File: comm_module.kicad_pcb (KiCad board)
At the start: 4 copper layers, 112.4 x 100.1 mm, 74 parts, among them J1 USB-231-ARY, J2 PH2.54-01-03PZS, J3 U.FL-R-SMT-1(80), J4 U.FL-R-SMT-1(80), J5 U.FL-R-SMT-1(80), J6 U.FL-R-SMT-1(80), J7 S3B-ZR-SM4A-TF(LF)(SN), J8 SMN-305-ARP7, J9 U.FL-R-SMT-1(80), Q1 BSS138PW,115, U1 MIC29302WU, U2 SIM7600E, U3 TXU0202DCUR, U4 TCA9406DCUR, X1 WJ500V-5.08-2P-14-00A

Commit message: First no error draft
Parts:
- removed J2: PH2.54-01-03PZS, pepy_sym_lib:[2x3_PIN_HEADER_STR]XUNPU PH2.54-01-03PZS
- removed J7: S3B-ZR-SM4A-TF(LF)(SN), pepy_sym_lib:[JST_1X3P_1_5MM_R_ANGLE]JST S3B-ZR-SM4A-TF(LF)(SN)
- removed R20: 0201WMF1002TEE, pepy_sym_lib:[RES_SMD_0201_0603Metric]
- added C26: CC0201KRX5R6BB104, pepy_sym_lib:[CAP_SMD_0201_0603Metric], F.Cu at (79.7, 86.3)
- added C27: CC0402KRX7R7BB104, pepy_sym_lib:[CAP_SMD_0402_1005Metric], F.Cu at (85.1, 55.7)
- added J10: PZ254V-11-06P, pepy_sym_lib:[6P_HEADER_STR]XFCN PZ254V-11-06P, F.Cu at (117.5, 50.0)
- added R24: 0805W8F1004T5E, pepy_sym_lib:[RES_SMD_0805_2012Metric], F.Cu at (69.8, 71.1)
- added R25: 0805W8F0000T5E, pepy_sym_lib:[RES_SMD_0805_2012Metric], F.Cu at (81.5, 56.5)
- added R26: 0402WGF2201TCE, pepy_sym_lib:[RES_SMD_0402_1005Metric], F.Cu at (115.0, 53.8)
- added R27: 0402WGF2201TCE, pepy_sym_lib:[RES_SMD_0402_1005Metric], F.Cu at (119.6, 50.8)
- added R28: 0805W8F0000T5E, pepy_sym_lib:[RES_SMD_0805_2012Metric], F.Cu at (81.5, 54.8)
- added TP1: DCD, pepy_sym_lib:[TEST_POINT]TestPoint_Pad_D1.0mm, F.Cu at (94.9, 55.3)
- added TP2: RI, pepy_sym_lib:[TEST_POINT]TestPoint_Pad_D1.0mm, F.Cu at (94.9, 52.4)
- added TP3: DTR, pepy_sym_lib:[TEST_POINT]TestPoint_Pad_D1.0mm, F.Cu at (91.6, 55.3)
- added TP4: RTS, pepy_sym_lib:[TEST_POINT]TestPoint_Pad_D1.0mm, F.Cu at (100.3, 49.7)
- added TP5: CTS, pepy_sym_lib:[TEST_POINT]TestPoint_Pad_D1.0mm, F.Cu at (98.3, 50.7)
- added TP6: SIM_STAT, pepy_sym_lib:[TEST_POINT]TestPoint_Pad_D1.0mm, F.Cu at (114.3, 79.2)
- added TP7: nRST, pepy_sym_lib:[TEST_POINT]TestPoint_Pad_D1.0mm, F.Cu at (78.2, 61.8)
- C16: value CC1206KKX7RDBB102 -> CC0201KRX5R6BB104; footprint pepy_sym_lib:[CAP_SMD_1206_3216Metric] -> pepy_sym_lib:[CAP_SMD_0201_0603Metric]
- J3, J4, J5, J6, J9: value U.FL-R-SMT-1(80) -> U.FLRSMT1
- R10: value RC0201FR-0733RL -> 0805W8F0000T5E; footprint pepy_sym_lib:[RES_SMD_0201_0603Metric] -> pepy_sym_lib:[RES_SMD_0805_2012Metric]
- R15: value 0805W8F1004T5E -> 0402WGF2201TCE; footprint pepy_sym_lib:[RES_SMD_0805_2012Metric] -> pepy_sym_lib:[RES_SMD_0402_1005Metric]
- R2: value 0402WGF0000TCE -> 0402WGF2201TCE
- R6: value RC0201FR-071ML -> 0805W8F0000T5E; footprint pepy_sym_lib:[RES_SMD_0201_0603Metric] -> pepy_sym_lib:[RES_SMD_0805_2012Metric]
- moved R2 69.6 mm to (123.4, 54.0), turned to 0 degrees
- moved C16 63.7 mm to (79.2, 79.3)
- moved R6 39.2 mm to (81.5, 58.2), turned to 180 degrees
- moved C1 37.6 mm to (76.6, 35.1), turned to 0 degrees
- moved R15 35.0 mm to (123.4, 51.2)
- moved D2 34.7 mm to (70.9, 32.0), turned to -90 degrees
- moved C3 33.4 mm to (72.7, 33.5), turned to -90 degrees
- moved R10 31.3 mm to (81.5, 53.1)
- moved R4 30.9 mm to (68.5, 32.1), turned to 0 degrees
- moved R5 28.7 mm to (66.5, 32.1), turned to 0 degrees
- moved R1 27.5 mm to (66.7, 42.2)
- moved C20 24.6 mm to (57.8, 75.7), turned to 180 degrees
- moved C25 23.9 mm to (121.1, 50.0), turned to 90 degrees
- moved C15 23.4 mm to (114.1, 56.6), turned to 180 degrees
- moved D1 20.7 mm to (63.9, 52.8)
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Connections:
- net /D+_COMM renamed /DCOMM+
- net /D-_COMM renamed /DCOMM-
- net Net-(D3-I/O1-Pad1) renamed /DFILT-
- net Net-(D3-I/O2-Pad3) renamed /DFILT+
- C10 pad 2: VDD_3V3 -> /1V8_COMM
- C11 pad 2: Net-(C11-Pad2) -> /MAIN_ANT
- C12 pad 2: Net-(C12-Pad2) -> /AUX_ANT
- C15 pad 2: /1V8_COMM -> /VDD_3V3
- C16 pad 1: Earth_UART -> GND
- C16 pad 2: GND -> /1V8_COMM
- C25 pad 1: VDD_3V3 -> /VDD_3V3
- D5 pad 1: /SIM_DATA -> /SIM_VCC
- D5 pad 3: /SIM_VCC -> /SIM_RST
- D5 pad 4: /SIM_RST -> /SIM_CLK
- D5 pad 5: /SIM_CLK -> /SIM_DATA
- Q1 pad 1: /NETFLIGHT -> /NETLIGHT
- R10 pad 1: /SIM_VCC -> Net-(C27-Pad2)
- R10 pad 2: Net-(U2A-USIM_VDD) -> /VDD_3V3
- R15 pad 1: Earth_UART -> /COMM_SCL
- R15 pad 2: GND -> /1V8_COMM
- R16 pad 2: /1V8_COMM -> /VDD_AUX
- R18 pad 2: /SIM_VCC -> Net-(C27-Pad2)
- R2 pad 1: /EN -> /COMM_SDA
- R2 pad 2: Net-(U1-EN) -> /1V8_COMM
- R21 pad 2: /NETFLIGHT -> /NETLIGHT
- R22 pad 2: /NETFLIGHT -> /NETLIGHT
- R23 pad 2: VDD_3V3 -> /VDD_COMM
- R6 pad 1: Earth_USB -> Net-(C27-Pad2)
- R6 pad 2: GND -> /1V8_COMM
- R7 pad 1: Net-(C11-Pad2) -> /MAIN_ANT
- R8 pad 1: Net-(C12-Pad2) -> /AUX_ANT
- U2 pad 20: Net-(U2A-USIM_VDD) -> /SIM_VCC
- U2 pad 4: /nRST -> Net-(U2A-RESET)
- U2 pad 44: unconnected-(U2B-VDD_AUX-Pad44) -> /VDD_AUX
- U3 pad 1: /M_RX_S_TX_1V8 -> /M_TX_S_RX
- U3 pad 3: VDD_3V3 -> /1V8_COMM
- U3 pad 4: /M_RX_S_TX -> /M_TX_S_RX_1V8
- U3 pad 5: /M_TX_S_RX -> /M_RX_S_TX_1V8
- U3 pad 6: VDD_3V3 -> /1V8_COMM
- U3 pad 7: /1V8_COMM -> /VDD_3V3
- U3 pad 8: /M_TX_S_RX_1V8 -> /M_RX_S_TX
- U4 pad 6: Net-(U4-OE) -> /1V8_COMM
- U4 pad 7: VDD_3V3 -> /VDD_3V3
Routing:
- net GND: track 0.00 -> 118.3 mm, vias 0 -> 86
- net /1V8_COMM: track 0.00 -> 96.1 mm
- net /VDD_3V3: track 0.00 -> 74.4 mm
- net /VDD_COMM: track 0.00 -> 48.4 mm, vias 0 -> 22
- net Earth_SIM: track 0.00 -> 45.4 mm
- net /VBUS: track 0.00 -> 38.5 mm, vias 0 -> 1
- net /COMM_SCL: track 0.00 -> 34.7 mm, vias 0 -> 2
- net /COMM_SDA: track 0.00 -> 29.1 mm, vias 0 -> 2
- net /M_RX_S_TX_1V8: track 0.00 -> 22.6 mm
- net /SIM_VCC: track 0.00 -> 21.4 mm
- net Earth_USB: track 0.00 -> 21.1 mm
- net /VDD_AUX: track 0.00 -> 19.6 mm
- net /DCOMM-: track 0.00 -> 19.1 mm
- net /DCOMM+: track 0.00 -> 19.1 mm
- net /SIM_DATA: track 0.00 -> 18.3 mm, vias 0 -> 2
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- added copper zone on B.Cu, net /VBUS
- added copper zone on F.Cu, net /VBUS
- added copper zone on B.Cu, net /VDD_COMM
- added copper zone on F.Cu, net /VDD_COMM
- added copper zone on In1.Cu, net GND
- added copper zone on In2.Cu, net GND
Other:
- board size 112.4 x 100.1 mm -> 73.7 x 65.6 mm
- board text added: "0"
- board text added: "0 mm"
- board text added: "0.01 mm"
- board text added: "0.0152 mm"
- board text added: "0.02"
- board text added: "0.035 mm"
- board text added: "0.0994 mm"
- board text added: "1"
- board text added: "1.265 mm"
- board text added: "3.3"
- board text added: "4.1"
- board text added: "4.5"
- board text added: "B.Cu"
- board text added: "B.Mask"
- board text added: "B.Paste"
- board text added: "B.Silkscreen"
- board text added: "Bottom Silk Screen"
- board text added: "Bottom Solder Mask"
- board text added: "Bottom Solder Paste"
- board text added: "Color"
- board text added: "Dielectric"
- board text added: "Epsilon R"
- board text added: "F.Cu"
- board text added: "F.Mask"
- board text added: "F.Paste"
- board text added: "F.Silkscreen"
- board text added: "FR4"
- board text added: "In1.Cu"
- board text added: "In2.Cu"
- board text added: "Layer Name"
- board text added: "Loss Tangent"
- board text added: "Material"
- board text added: "Not specified"
- board text added: "Thickness (mm)"
- board text added: "Top Silk Screen"
- board text added: "Top Solder Mask"
- board text added: "Top Solder Paste"
- board text added: "Type"
- board text added: "copper"
- board text added: "core"
- board text added: "prepreg"

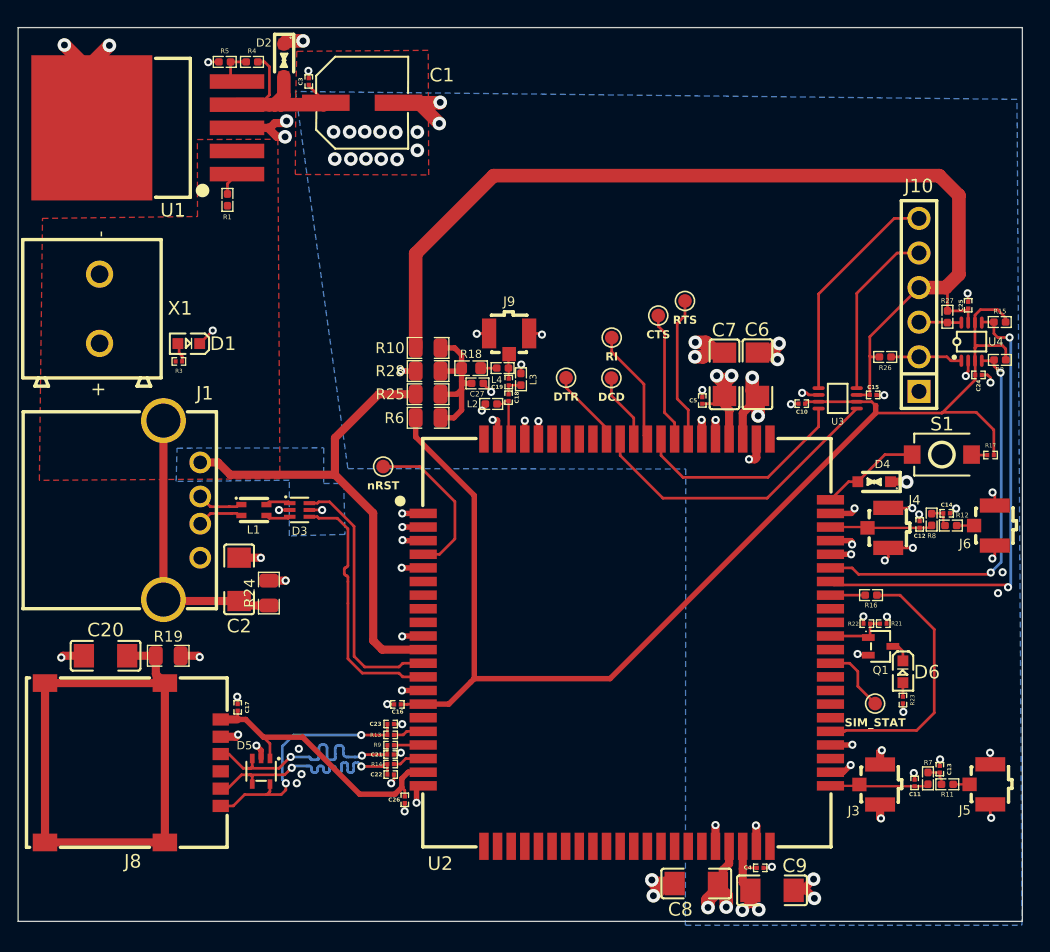
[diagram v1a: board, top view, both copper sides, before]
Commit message: Reannotation
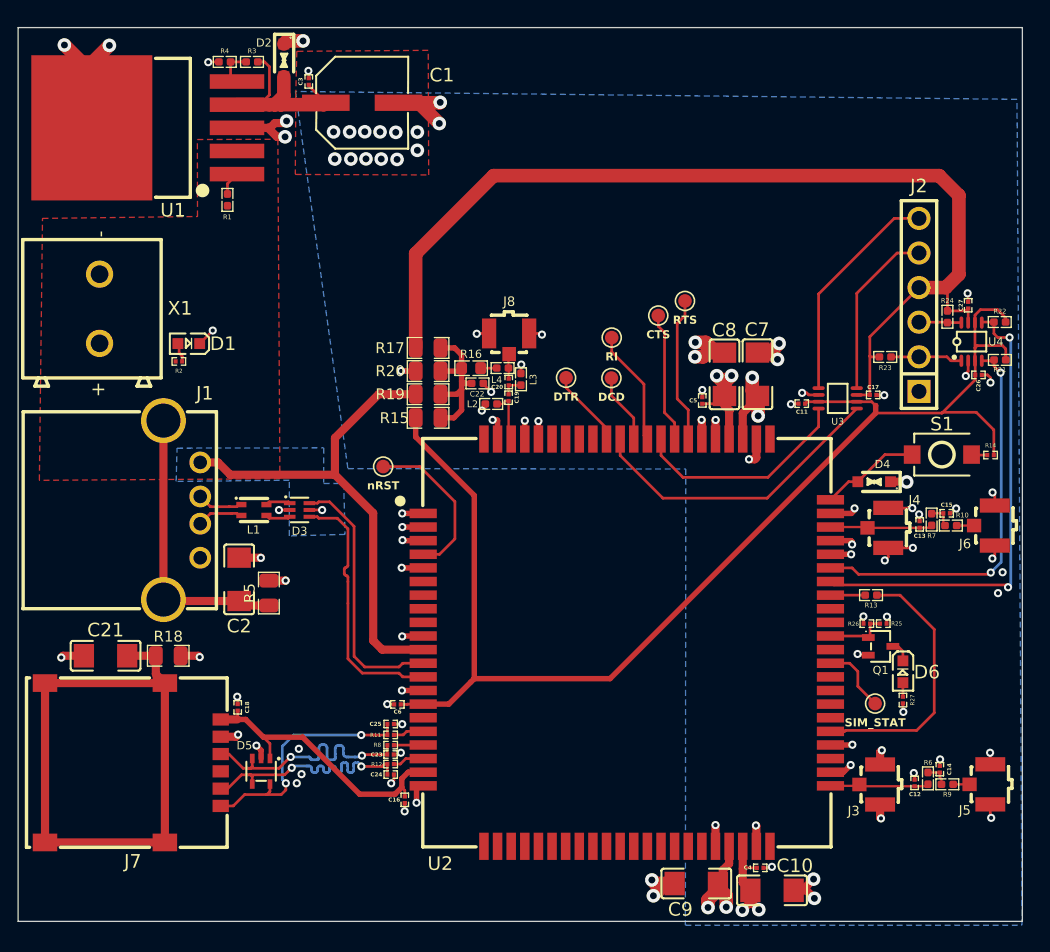
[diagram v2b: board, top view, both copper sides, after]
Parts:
- renumbered C9 to C10, C10 to C11, C11 to C12, C12 to C13, C13 to C14, C14 to C15, C26 to C16, C15 to C17, C17 to C18, C18 to C19, C19 to C20, C20 to C21, C27 to C22, C21 to C23, C22 to C24, C23 to C25, C24 to C26, C25 to C27, C16 to C6, C6 to C7, C7 to C8, C8 to C9, J10 to J2, J8 to J7, J9 to J8, R12 to R10, R13 to R11, R14 to R12, R16 to R13, R17 to R14, R6 to R15, R18 to R16, R10 to R17, R19 to R18, R25 to R19, R3 to R2, R28 to R20, R2 to R21, R15 to R22, R26 to R23, R27 to R24, R21 to R25, R22 to R26, R23 to R27, R4 to R3, R5 to R4, R24 to R5, R7 to R6, R8 to R7, R9 to R8, R11 to R9, TP7 to TP6, TP6 to TP7

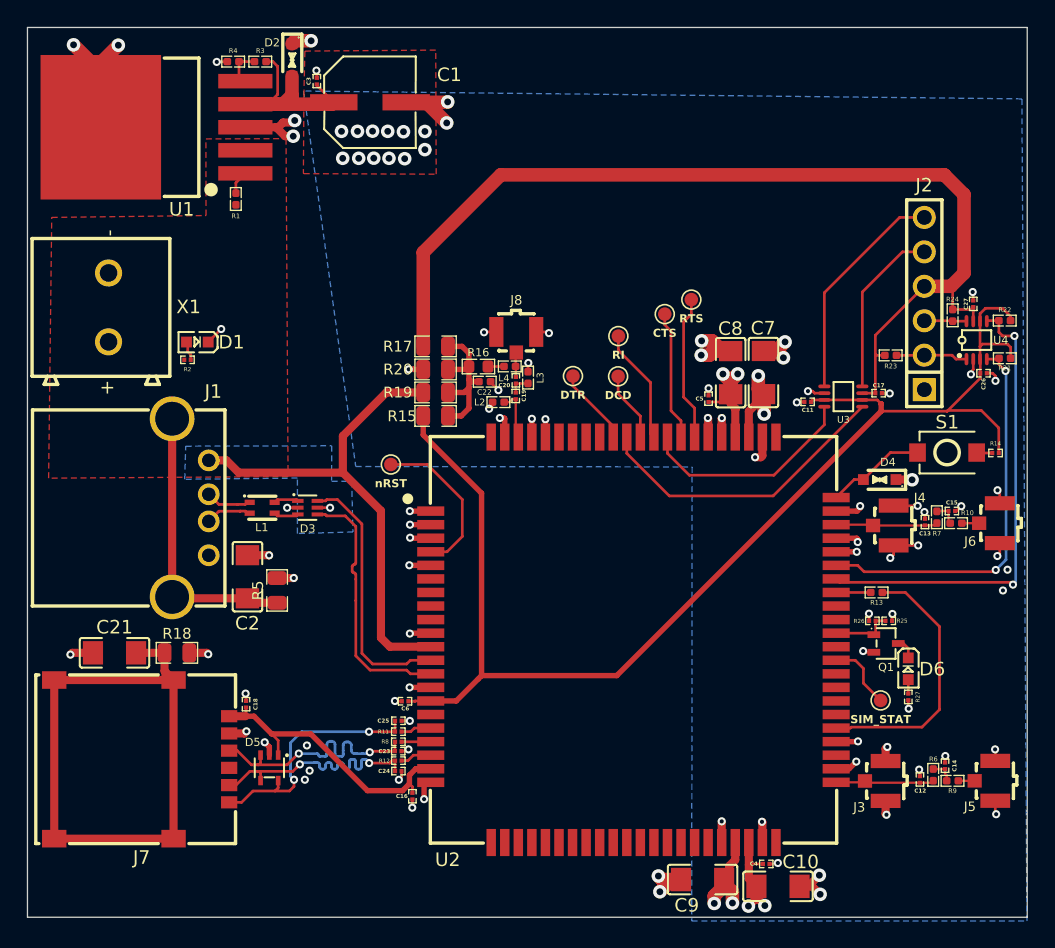
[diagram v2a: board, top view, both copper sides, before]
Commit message: Antenna polygon fixes and refinements
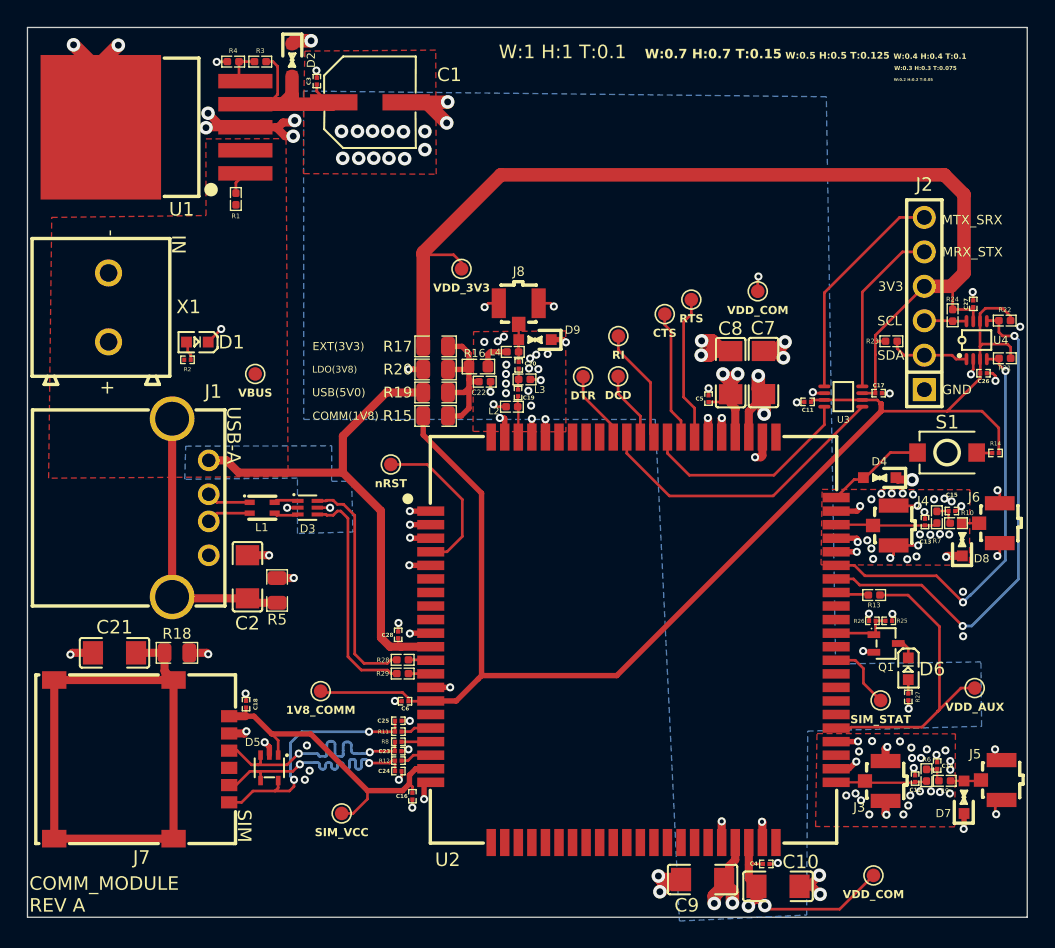
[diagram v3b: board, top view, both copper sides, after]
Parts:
- added C28: CC0201KRX5R6BB104, pepy_sym_lib:[CAP_SMD_0201_0603Metric], F.Cu at (78.7, 74.4)
- added D7: ESD56151W05, pepy_sym_lib:[ESD_PROT]WILLSEMI ESD56151W05-2TR, F.Cu at (120.4, 86.4)
- added D8: ESD56151W05, pepy_sym_lib:[ESD_PROT]WILLSEMI ESD56151W05-2TR, F.Cu at (120.3, 67.4)
- added D9: ESD56151W05, pepy_sym_lib:[ESD_PROT]WILLSEMI ESD56151W05-2TR, F.Cu at (88.8, 52.6)
- added R28: 0402WGF0000TCE, pepy_sym_lib:[RES_SMD_0402_1005Metric], F.Cu at (79.0, 76.2)
- added R29: 0402WGF0000TCE, pepy_sym_lib:[RES_SMD_0402_1005Metric], F.Cu at (79.0, 77.2)
- added TP10: 1V8_COMM, pepy_sym_lib:[TEST_POINT]TestPoint_Pad_D1.0mm, F.Cu at (73.0, 78.5)
- added TP11: VDD_3V3, pepy_sym_lib:[TEST_POINT]TestPoint_Pad_D1.0mm, F.Cu at (83.4, 47.4)
- added TP12: VBUS, pepy_sym_lib:[TEST_POINT]TestPoint_Pad_D1.0mm, F.Cu at (68.1, 55.1)
- added TP13: SIM_VCC, pepy_sym_lib:[TEST_POINT]TestPoint_Pad_D1.0mm, F.Cu at (74.5, 87.6)
- added TP14: VDD_COM, pepy_sym_lib:[TEST_POINT]TestPoint_Pad_D1.0mm, F.Cu at (105.2, 49.0)
- added TP8: VDD_COM, pepy_sym_lib:[TEST_POINT]TestPoint_Pad_D1.0mm, F.Cu at (113.7, 92.1)
- added TP9: VDD_AUX, pepy_sym_lib:[TEST_POINT]TestPoint_Pad_D1.0mm, F.Cu at (121.2, 78.3)
- moved J8 2.12 mm to (87.6, 50.7)
- moved C20 1.12 mm to (87.6, 54.5)
- moved L4 1.09 mm to (87.1, 53.5)
- moved L2 1.05 mm to (87.1, 57.6)
- moved R23 1.04 mm to (115.1, 52.7)
- moved TP3 0.75 mm to (92.3, 55.3)
- moved C14 0.58 mm to (118.4, 84.0)
- moved R9 0.57 mm to (119.0, 85.2)
- moved R6 0.50 mm to (117.7, 84.7)
- moved J5 0.47 mm to (122.4, 85.1)
- moved C12 0.36 mm to (116.8, 85.0)
- moved L3 0.31 mm to (88.0, 55.5), turned to 180 degrees
- moved C19 0.28 mm to (87.5, 56.5)
- moved R13 0.26 mm to (113.8, 71.5)
- moved D4 0.14 mm to (114.2, 62.8)
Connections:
- D3 pad 4: /DCOMM+ -> /DR+
- D3 pad 6: /DCOMM- -> /DR-
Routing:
- net /DCOMM-: track 19.1 -> 1.65 mm
- net /DCOMM+: track 19.1 -> 1.65 mm
- net /DR+: track 0.00 -> 17.0 mm
- net /DR-: track 0.00 -> 16.9 mm
- net GND: track 118.3 -> 129.6 mm, vias 86 -> 145
- net /VDD_COMM: track 48.4 -> 58.9 mm, vias 22 -> 23
- net /1V8_COMM: track 96.1 -> 102.9 mm
- net /VDD_3V3: track 74.4 -> 78.0 mm
- net /VDD_AUX: track 19.6 -> 23.1 mm
- net /SIM_VCC: track 21.4 -> 24.3 mm
- net /COMM_SCL: track 34.7 -> 37.4 mm
- net /COMM_SDA: track 29.1 -> 30.9 mm
- net Net-(D7-A): track 1.20 -> 2.74 mm
- net Net-(L4-Pad2): track 1.18 -> 2.39 mm
- net Net-(D9-A): track 1.83 -> 2.83 mm
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- added copper zone on F.Cu, net GND
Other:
- board text added: "3V3"
- board text added: "By:perseluspy"
- board text added: "COMM(1V8)"
- board text added: "COMM_MODULE REV A"
- board text added: "EXT(3V3)"
- board text added: "GND"
- board text added: "IN"
- board text added: "LDO(3V8)"
- board text added: "MRX_STX"
- board text added: "MTX_SRX"
- board text added: "SCL"
- board text added: "SDA"
- board text added: "SIM"
- board text added: "USB(5V0)"
- board text added: "USB-A"
- board text added: "W:0.2 H:0.2 T:0.05"
- board text added: "W:0.3 H:0.3 T:0.075"
- board text added: "W:0.4 H:0.4 T:0.1"
- board text added: "W:0.5 H:0.5 T:0.125"
- board text added: "W:0.7 H:0.7 T:0.15"
- board text added: "W:1 H:1 T:0.1"

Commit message: Rev A
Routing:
- net GND: track 129.6 -> 130.2 mm
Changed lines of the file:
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@@
 	)
 	(segment
-		(start 105.432922 61.287078)
-		(end 105.55 61.17)
-		(width 0.6)
-		(layer "F.Cu")
-		(net 2)
-	)
-	(segment
 		(start 81.09 67.259482)
 		(end 79.609482 67.259482)
@@
 	)
 	(segment
+		(start 106.68 61.3664)
+		(end 105.7464 61.3664)
+		(width 0.6)
+		(layer "F.Cu")
+		(net 2)
+	)
+	(segment
 		(start 79.580518 74.259482)
 		(end 79.55 74.29)
@@
 	)
 	(segment
+		(start 105.55 61.17)
+		(end 105.55 59.799482)
+		(width 0.6)
+		(layer "F.Cu")
+		(net 2)
+	)
+	(segment
 		(start 72.69 33.31)
 		(end 72.69 32.8)
@@
 	)
 	(segment
-		(start 105.55 61.17)
-		(end 105.55 59.799482)
-		(width 0.6)
-		(layer "F.Cu")
-		(net 2)
-	)
-	(segment
 		(start 99.55 92.43)
 		(end 98.14 92.43)
@@
 	)
 	(segment
-		(start 105.010687 61.287078)
-		(end 105.432922 61.287078)
-		(width 0.6)
-		(layer "F.Cu")
-		(net 2)
-	)
-	(segment
 		(start 109.2708 56.4896)
 		(end 109.387999 56.4896)
@@
 	)
 	(segment
+		(start 105.7464 61.3664)
+		(end 105.55 61.17)
+		(width 0.6)
+		(layer "F.Cu")
+		(net 2)
+	)
+	(segment
 		(start 69.16 68.51)
 		(end 69.17 68.52)
@@
 	)
 	(via
-		(at 105.010687 61.287078)
+		(at 106.68 61.3664)
 		(size 0.6)
 		(drill 0.3)
@@
 		(polygon
 			(pts
-				(xy 63.02 60.47) (xy 73.789339 60.442735) (xy 73.779311 63.06) (xy 75.26 63.06) (xy 75.35 66.8)
-				(xy 71.26 66.91) (xy 71.26 62.82) (xy 62.95 62.91)
+				(xy 63.02 60.47) (xy 73.789339 60.442735) (xy 73.780729 62.689831) (xy 74.149483 63.06) (xy 75.26 63.06)
+				(xy 75.35 66.8) (xy 71.26 66.91) (xy 71.26 63.8425) (xy 70.23756 62.831073) (xy 62.95 62.91)
 			)
 		)
@@
 		(polygon
 			(pts
-				(xy 71.71 34.28) (xy 71.7296 58.4962) (xy 97.645311 58.4962) (xy 99.431516 95.49) (xy 108.8136 95.0468)
-				(xy 108.8898 81.4832) (xy 121.7168 81.1276) (xy 121.666 76.3778) (xy 110.9472 76.5302) (xy 110.264223 34.700293)
+				(xy 71.71 34.28) (xy 71.725553 53.496202) (xy 81.508295 63.253059) (xy 94.580513 63.229007) (xy 99.279503 67.949013)
+				(xy 99.1108 94.7166) (xy 108.8136 95.0468) (xy 108.891668 84.429613) (xy 112.115599 81.2038) (xy 121.7168 81.1276)
+				(xy 121.666 76.3778) (xy 113.235215 76.337749) (xy 110.950739 74.064466) (xy 110.614507 39.264367)
+				(xy 105.5662 34.266582)
 			)
 		)
